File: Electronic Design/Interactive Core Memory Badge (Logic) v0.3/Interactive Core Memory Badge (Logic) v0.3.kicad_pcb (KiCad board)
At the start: 2 copper layers, 80.2 x 160.1 mm, 126 parts, among them J1 Conn_01x16_Female, J10 Conn_01x08_Female, J11 Conn_01x08_Female, J12 Conn_01x08_Female, J13 Conn_01x08_Female, J2 Conn_01x16_Female, J3 BM03B-PASS-1-TFT__LF__SN_, J4 Conn_01x02_Male, J5 Conn_01x04_Female, J6 Conn_01x08_Female, J7 Conn_01x04_Male, J8 Conn_01x08_Female, J9 Conn_02x06_Odd_Even, Q1 IRLML6344TRPBF, Q10 MMBT4401LT1G, Q11 MMBT4403LT1G, Q12 MMBT4401LT1G, Q13 MMBT4403LT1G, Q14 MMBT4401LT1G, Q15 MMBT4403LT1G, Q16 MMBT4401LT1G, Q17 MMBT4403LT1G, Q18 MMBT4401LT1G, Q19 MMBT4403LT1G, Q2 MMBT4403LT1G, Q20 MMBT4401LT1G, Q21 MMBT4403LT1G, Q22 MMBT4401LT1G, Q3 MMBT4401LT1G, Q4 MMBT4401LT1G, Q5 MMBT4403LT1G, Q6 MMBT4401LT1G, Q7 MMBT4403LT1G, Q8 MMBT4401LT1G, Q9 MMBT4403LT1G, SW1 SW_DPDT_x2, U1 LD1117S33TR_SOT223, U10 M24C01-RMN, U2 Teensy-LC, U3 LM393, U4 74HC02, U5 MCP23017_SO, U6 MCP23017_SO, U7 SN74LV1T125DBVR, U8 74AC04, U9 74AC04, X1 SAO_v169bis, X2 SAO_v169bis, X3 SAO_v169bis

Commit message: Footprint verification and refinement
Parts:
- J1, J2: value Conn_01x16_Female -> SSW-116-22-F-S-VS‎
- J5: value Conn_01x04_Female -> SSW-104-22-L-S-VS
- J9: value Conn_02x06_Odd_Even -> TSM-106-03-T-DV‎
- X1, X2, X3: value SAO_v169bis -> SFH11-NBPC-D03-ST-BK
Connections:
- J3 pad 1: -BATT -> +BATT
- J3 pad 3: +BATT -> -BATT
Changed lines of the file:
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@@
       (effects (font (size 1 1) (thickness 0.15)))
     )
-    (fp_text value Conn_01x04_Female (at 0 6.68 90) (layer F.Fab)
+    (fp_text value SSW-104-22-L-S-VS (at 0 6.68 90) (layer F.Fab)
       (effects (font (size 1 1) (thickness 0.15)))
     )
@@
       (effects (font (size 1 1) (thickness 0.15)))
     )
-    (fp_text value SAO_v169bis (at 0 -8.509) (layer F.Fab)
+    (fp_text value SFH11-NBPC-D03-ST-BK (at 0 -8.509) (layer F.Fab)
       (effects (font (size 1 1) (thickness 0.15)))
     )
@@
     (fp_arc (start 2 -5) (end 2 -5.1) (angle -180) (layer F.SilkS) (width 0.2))
     (pad 1 smd rect (at 2 -3.075 90) (size 1 2.9) (layers F.Cu F.Paste F.Mask)
-      (net 3 -BATT))
+      (net 122 +BATT))
     (pad 2 smd rect (at 0 -3.075 90) (size 1 2.9) (layers F.Cu F.Paste F.Mask)
       (net 125 "Net-(J3-Pad2)"))
     (pad 3 smd rect (at -2 -3.075 90) (size 1 2.9) (layers F.Cu F.Paste F.Mask)
-      (net 122 +BATT))
+      (net 3 -BATT))
     (pad MH1 np_thru_hole circle (at -4.25 -1.825 90) (size 2.326 0) (drill 2.326) (layers *.Cu *.Mask))
     (pad MH2 np_thru_hole circle (at 4.2 -1.825 90) (size 0.9 0) (drill 0.9) (layers *.Cu *.Mask))
@@
       (effects (font (size 1 1) (thickness 0.15)))
     )
-    (fp_text value SAO_v169bis (at 0 -8.509) (layer F.Fab)
+    (fp_text value SFH11-NBPC-D03-ST-BK (at 0 -8.509) (layer F.Fab)
       (effects (font (size 1 1) (thickness 0.15)))
     )
@@
       (effects (font (size 1 1) (thickness 0.15)))
     )
-    (fp_text value SAO_v169bis (at 0 -8.509) (layer F.Fab)
+    (fp_text value SFH11-NBPC-D03-ST-BK (at 0 -8.509) (layer F.Fab)
       (effects (font (size 1 1) (thickness 0.15)))
     )
@@
       (effects (font (size 1 1) (thickness 0.15)))
     )
-    (fp_text value Conn_01x16_Female (at 0 21.38) (layer F.Fab)
+    (fp_text value SSW-116-22-F-S-VS‎ (at 0 21.38) (layer F.Fab)
       (effects (font (size 1 1) (thickness 0.15)))
     )
@@
       (effects (font (size 1 1) (thickness 0.15)))
     )
-    (fp_text value Conn_01x16_Female (at 0 21.38) (layer F.Fab)
+    (fp_text value SSW-116-22-F-S-VS‎ (at 0 21.38) (layer F.Fab)
       (effects (font (size 1 1) (thickness 0.15)))
     )
@@
       (effects (font (size 1 1) (thickness 0.15)))
     )
-    (fp_text value Conn_02x06_Odd_Even (at 0 8.68) (layer F.Fab)
+    (fp_text value TSM-106-03-T-DV‎ (at 0 8.68) (layer F.Fab)
       (effects (font (size 1 1) (thickness 0.15)))
     )

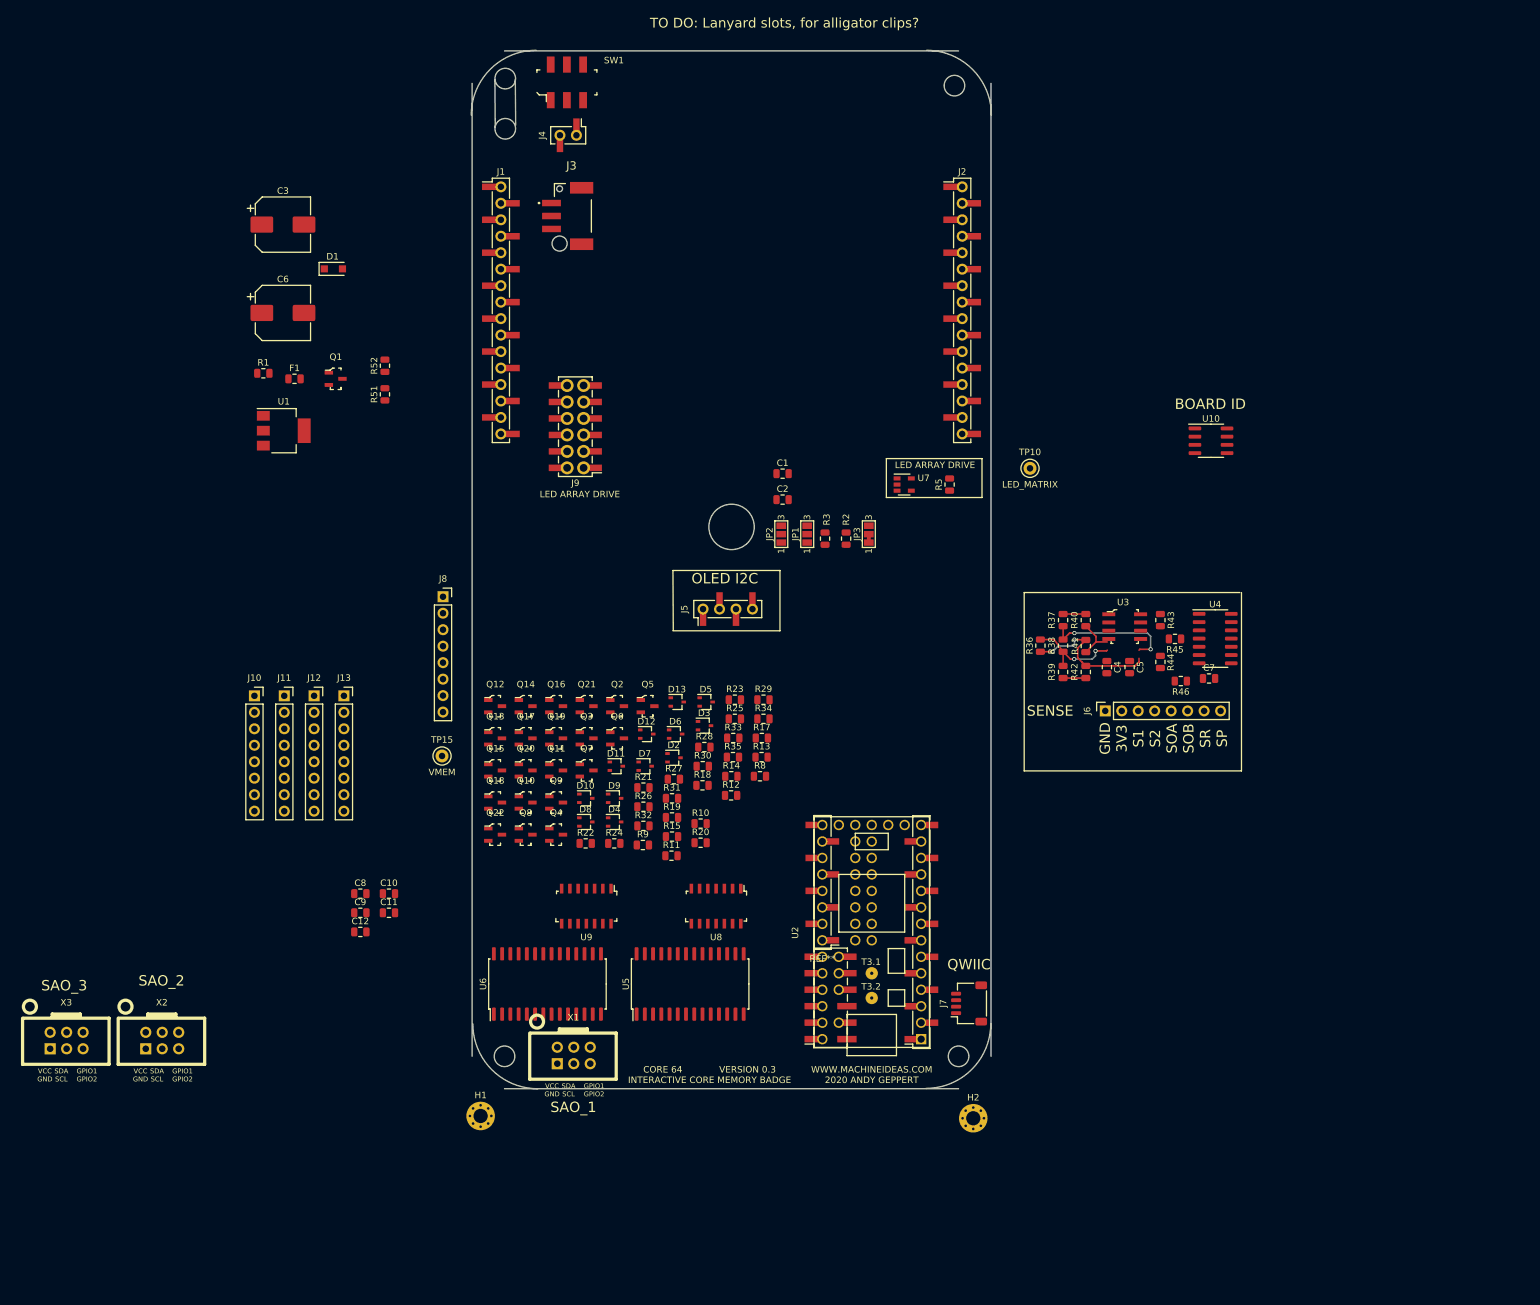
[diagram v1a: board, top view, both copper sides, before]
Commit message: Embiggen to 85x170mm
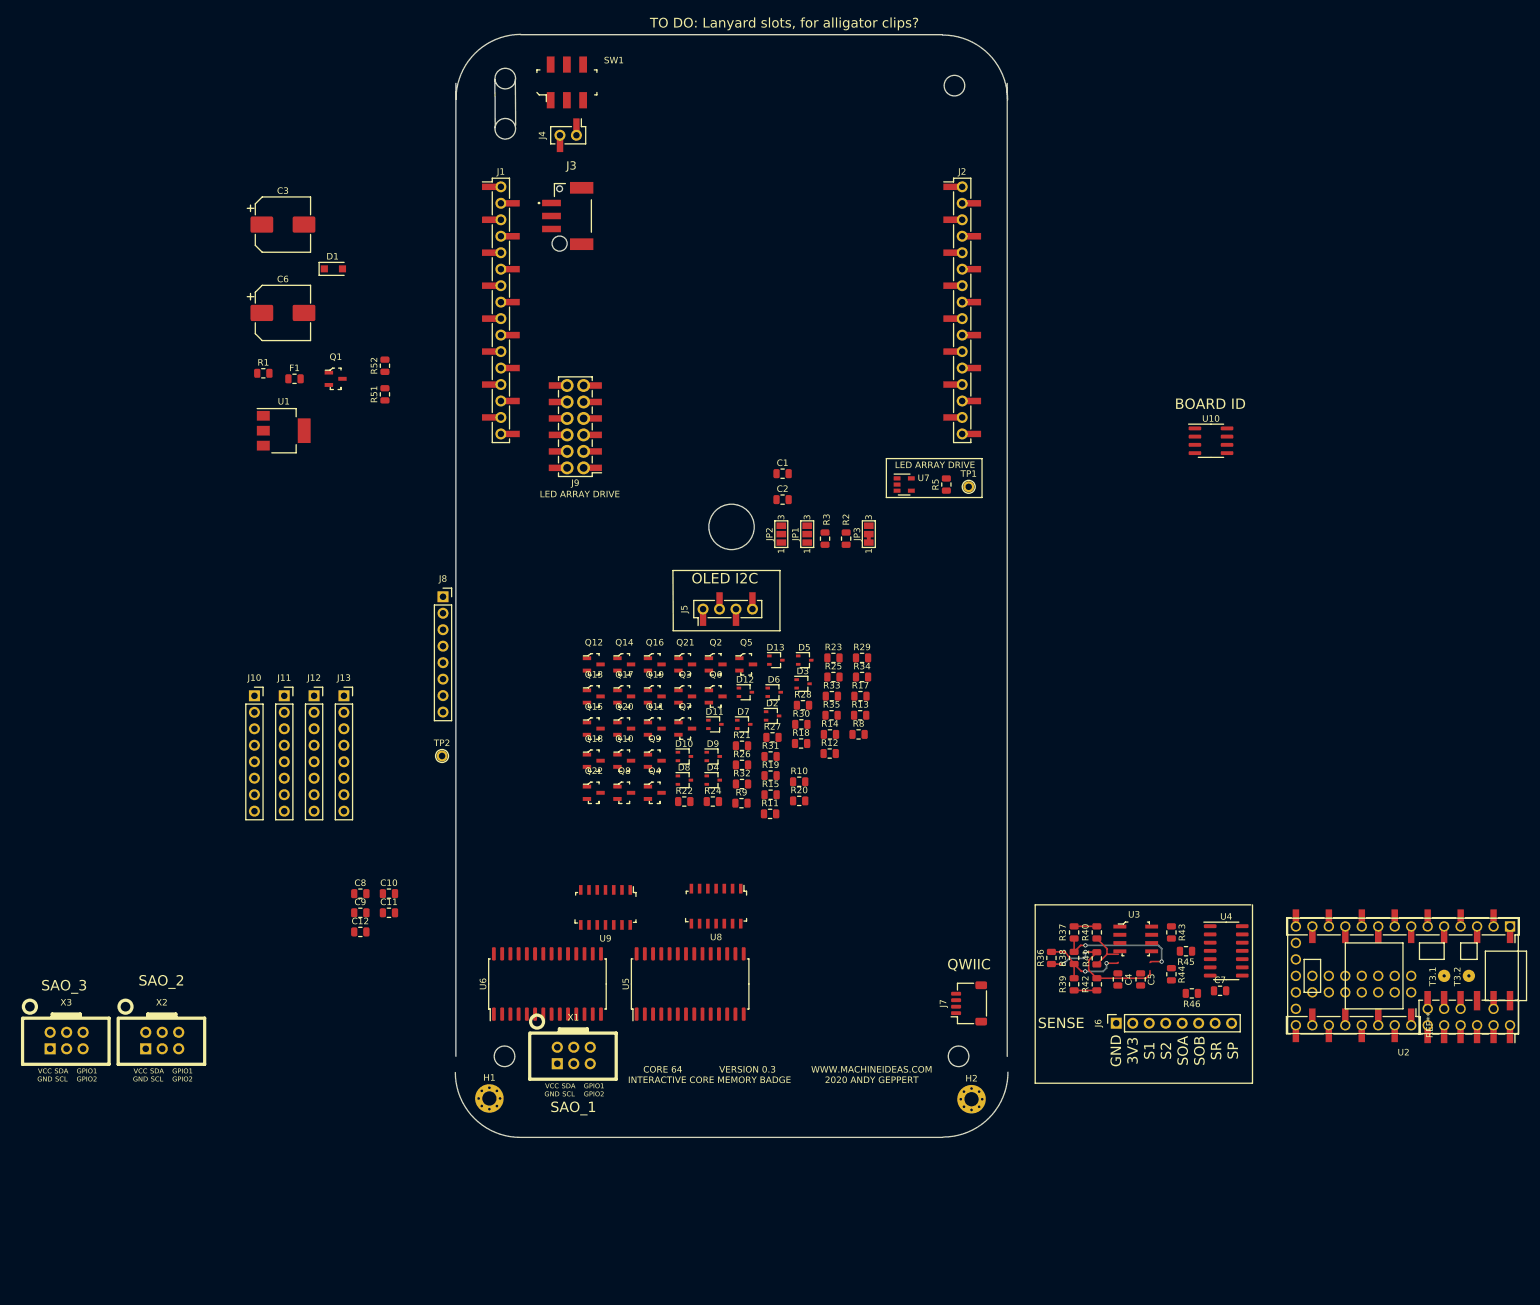
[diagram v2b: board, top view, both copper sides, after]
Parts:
- removed TP10: LED_MATRIX, TestPoint:TestPoint_Keystone_5000-5004_Miniature
- removed TP15: VMEM, TestPoint:TestPoint_Keystone_5000-5004_Miniature
- added TP1: LED_MATRIX, TestPoint:TestPoint_THTPad_D1.7mm_Drill1.0mm, F.Cu at (36.6, 27.2)
- added TP2: VMEM, TestPoint:TestPoint_THTPad_D1.7mm_Drill1.0mm, F.Cu at (-44.6, 68.7)
- moved U2 82.2 mm to (103.5, 102.6), turned to 180 degrees
- moved C4 48.2 mm to (59.6, 103.2)
- moved C5 48.2 mm to (63.1, 103.2)
- moved C7 48.2 mm to (75.3, 104.9)
- moved J6 48.2 mm to (59.3, 109.9)
- moved R36 48.2 mm to (49.3, 99.8)
- moved R37 48.2 mm to (52.8, 95.9)
- moved R38 48.2 mm to (52.8, 99.8)
- moved R39 48.2 mm to (52.8, 103.9)
- moved R40 48.2 mm to (56.3, 95.9)
- moved R41 48.2 mm to (56.3, 99.9)
- moved R42 48.2 mm to (56.3, 103.9)
- moved R43 48.2 mm to (67.8, 95.9)
- moved U3 48.2 mm to (62.3, 96.9)
- moved R45 48.2 mm to (70.1, 98.8)
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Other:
- board size 80.2 x 160.1 mm -> 85.2 x 170.1 mm

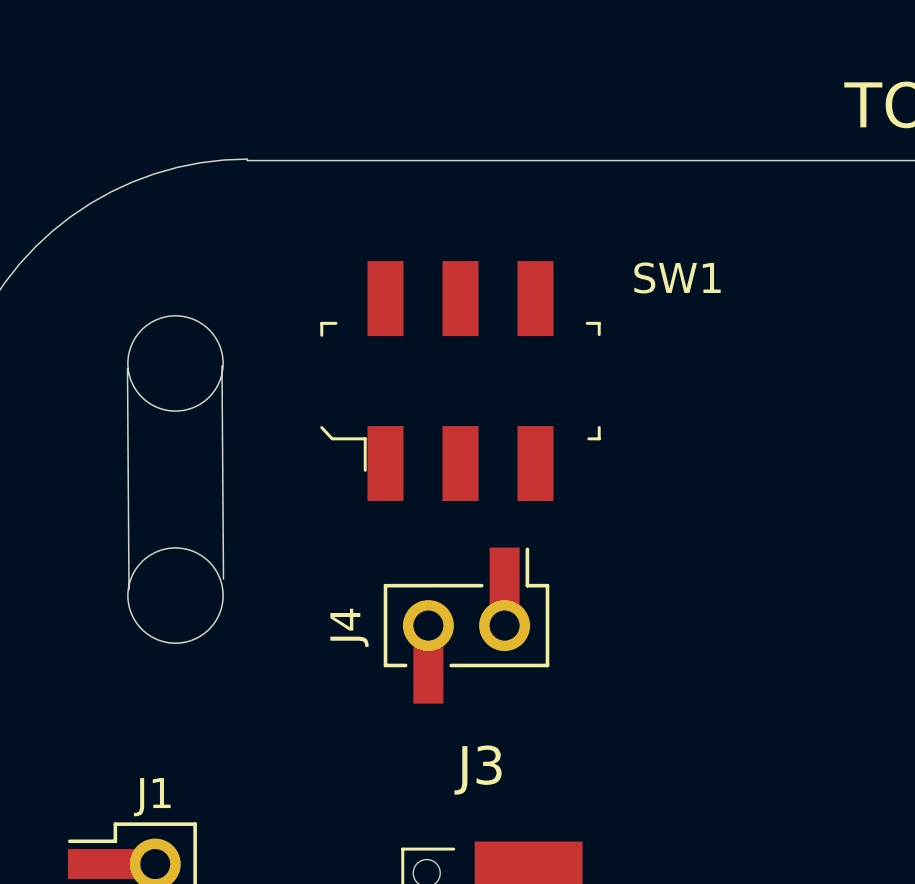
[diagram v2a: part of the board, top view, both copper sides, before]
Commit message: Update library refs (OneDrive to Dropbox)
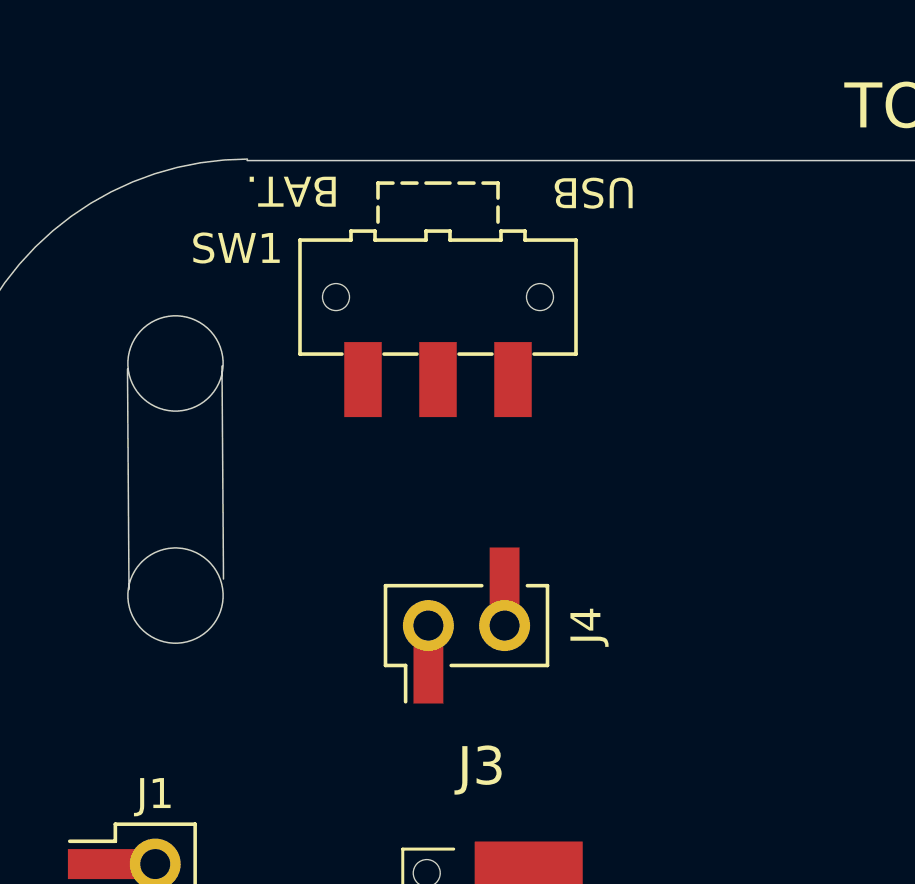
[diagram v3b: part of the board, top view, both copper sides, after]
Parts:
- SW1: value SW_DPDT_x2 -> JS102011SAQN; footprint Digikey:Switch_Slide_JS202011SCQN -> Button_Switch_SMD:SW_SPDT_CK-JS102011SAQN
- X1, X2, X3: value SFH11-NBPC-D03-ST-BK -> SAO_conn_SFH11-NBPC-D03-ST-BK
- moved SW1 2.90 mm to (-26.1, -38.0), turned to 180 degrees
- turned J4 to 90 degrees
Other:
- board text added: "BAT."
- board text added: "USB"
